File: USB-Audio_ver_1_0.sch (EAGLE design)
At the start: 61 parts, among them IC1 PCM2904DB, IC2 OPA2353UA, IC3 OPA2353UA, IC4 REG103GA-A

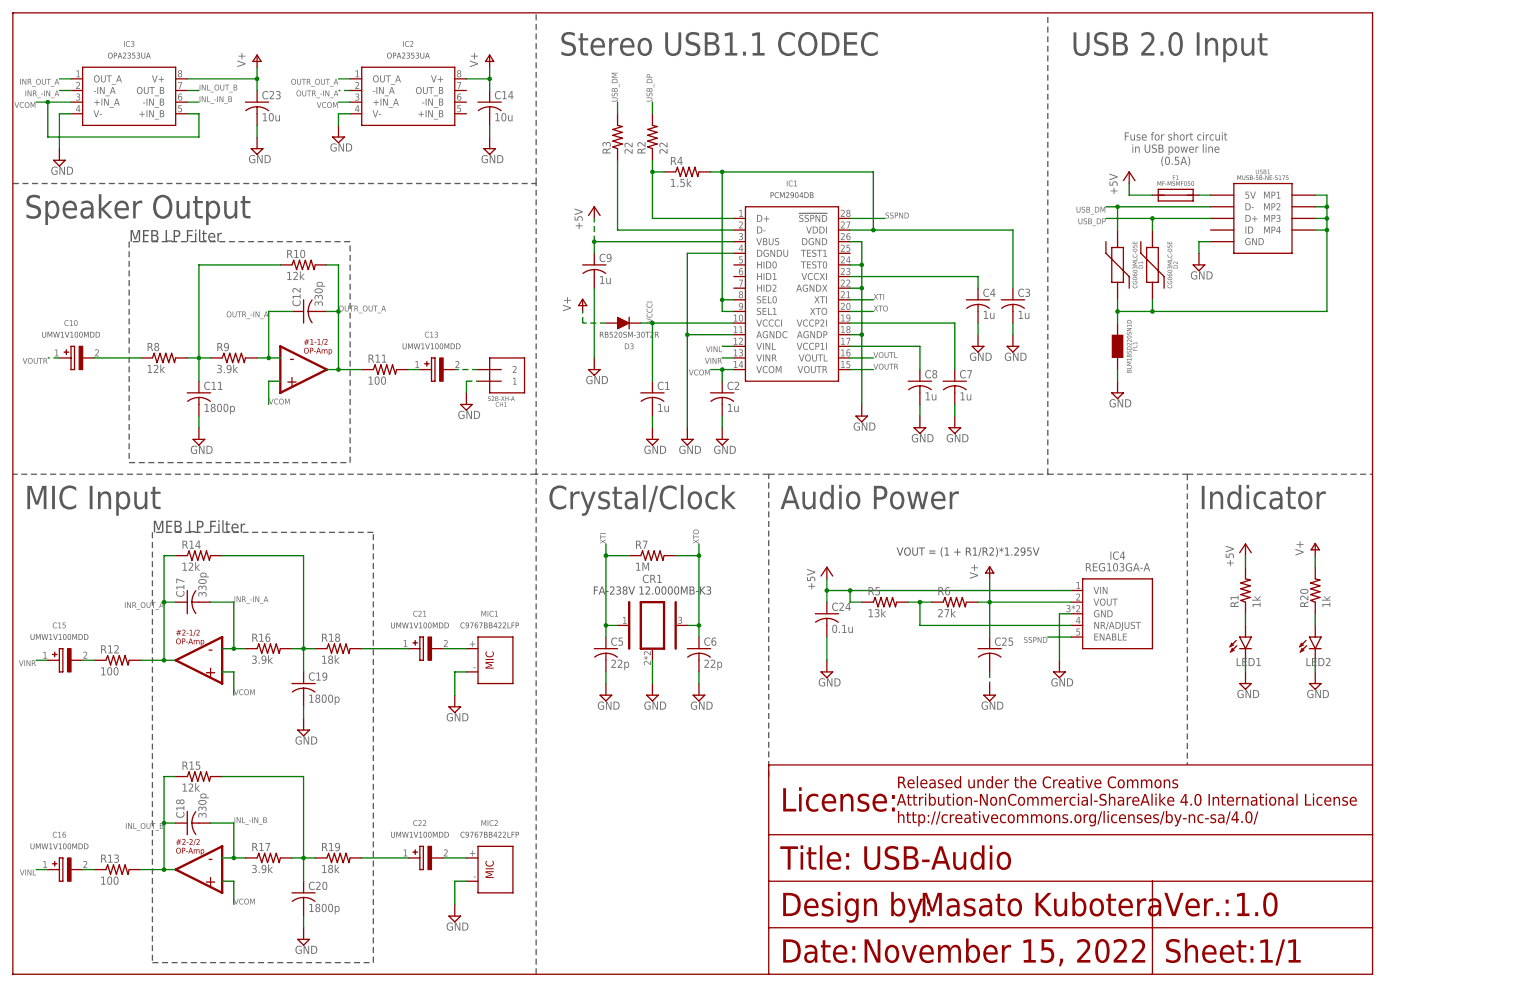
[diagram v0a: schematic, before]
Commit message: Modified power supply and silk printing
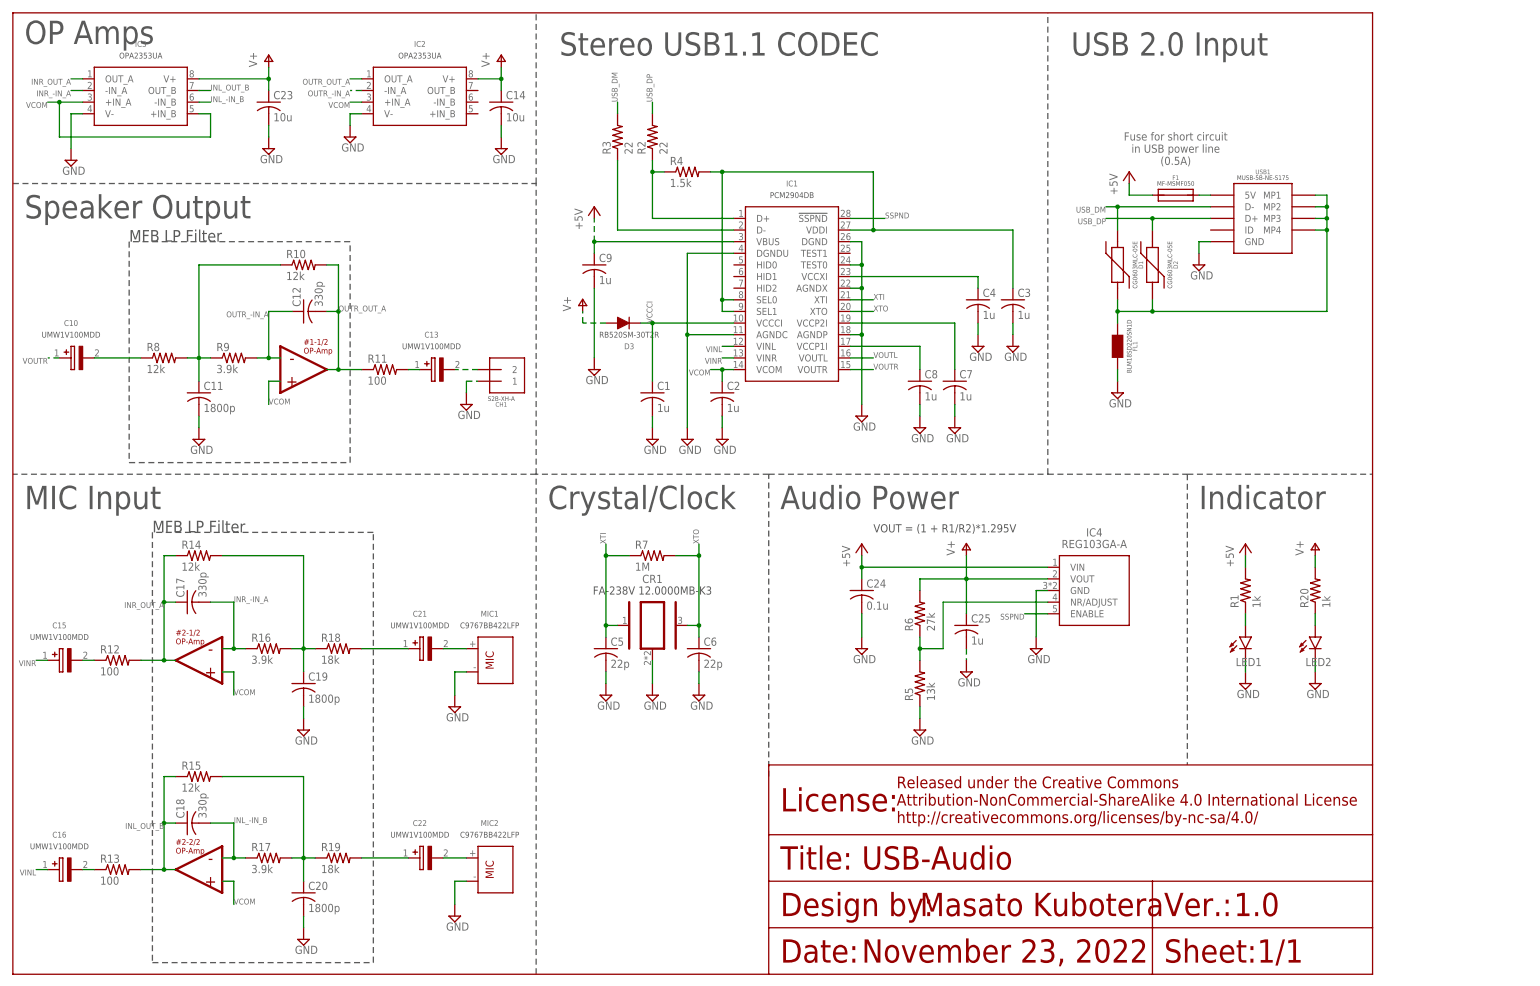
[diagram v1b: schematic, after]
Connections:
- net +5V: no longer R5.1
- net GND: now also R5.1
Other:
- note added: "November 23, 2022"
- note added: "OP Amps"
- note removed: "November 15, 2022"
- moved on the sheet: C14, C23, C24, C25, IC2, IC3, IC4, R5, R6
